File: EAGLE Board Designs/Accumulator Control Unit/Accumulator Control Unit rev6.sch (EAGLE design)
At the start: 261 parts, among them J1 CONNECTOR-12_MF_T_V_, J2 CONNECTOR-6_μF_T_V_BLACK, J3 CONNECTOR-4_μF_T_V_BLACK, J4 CONNECTOR-2_MF_T_V_, J5 CONNECTOR-8_μF_T_V_BLACK, J6 CONNECTOR-16_MF_T_V_, J9 CONNECTOR-2_MF_T_V_, Q1 TRANSISTOR_N_MOS__PMV15ENEA, Q2 TRANSISTOR_N_MOS__PMV15ENEA, Q3 TRANSISTOR_N_MOS__PMV15ENEA, Q4 TRANSISTOR_N_MOS__PMV15ENEA, T1 TRANSFORMER_HM2112ZNLT_AIRGAP, U1 VOLTAGE_REGULATOR_SOT-223_3.3V, U10 TCAN1051HQV-Q1, U11 OPAMP_1_CHANNEL_OPA991, U12 OPAMP_1_CHANNEL_OPA991, U13 OPAMP_1_CHANNEL_OPA991, U14 RELAY_SOLIDSTATE_NO_DIP-4, U15 LM555, U16 OPAMP_1_CHANNEL_OPA991, U17 MAX7404, U18 OPAMP_1_CHANNEL_OPA991, U19 MAX7404, U2 RELAY_SOLIDSTATE_NO_DIP-4, U20 LOGICGATE_BUFFER, U21 ADM8316WBX30, U22 OPAMP_1_CHANNEL_OPA991, U23 LOGICGATE_AND_DCK3, U24 LOGICGATE_AND_DCK3, U25 LOGICGATE_AND_DCK3, U26 OPAMP_1_CHANNEL_OPA991, U27 ADG1423, U28 OPAMP_1_CHANNEL_OPA991, U29 MAX7404, U3 RELAY_SOLIDSTATE_NO_DIP-4, U30 OPAMP_1_CHANNEL_OPA991, U31 MAX7404, U32 LTC6820, U33 OPAMP_1_CHANNEL_OPA991, U4 OPAMP_1_CHANNEL_OPA991, U5 OPAMP_1_CHANNEL_OPA991, U6 TCAN1051HQV-Q1, U7 LTC6820, U8 OPAMP_1_CHANNEL_OPA991, U9 OPAMP_1_CHANNEL_OPA991

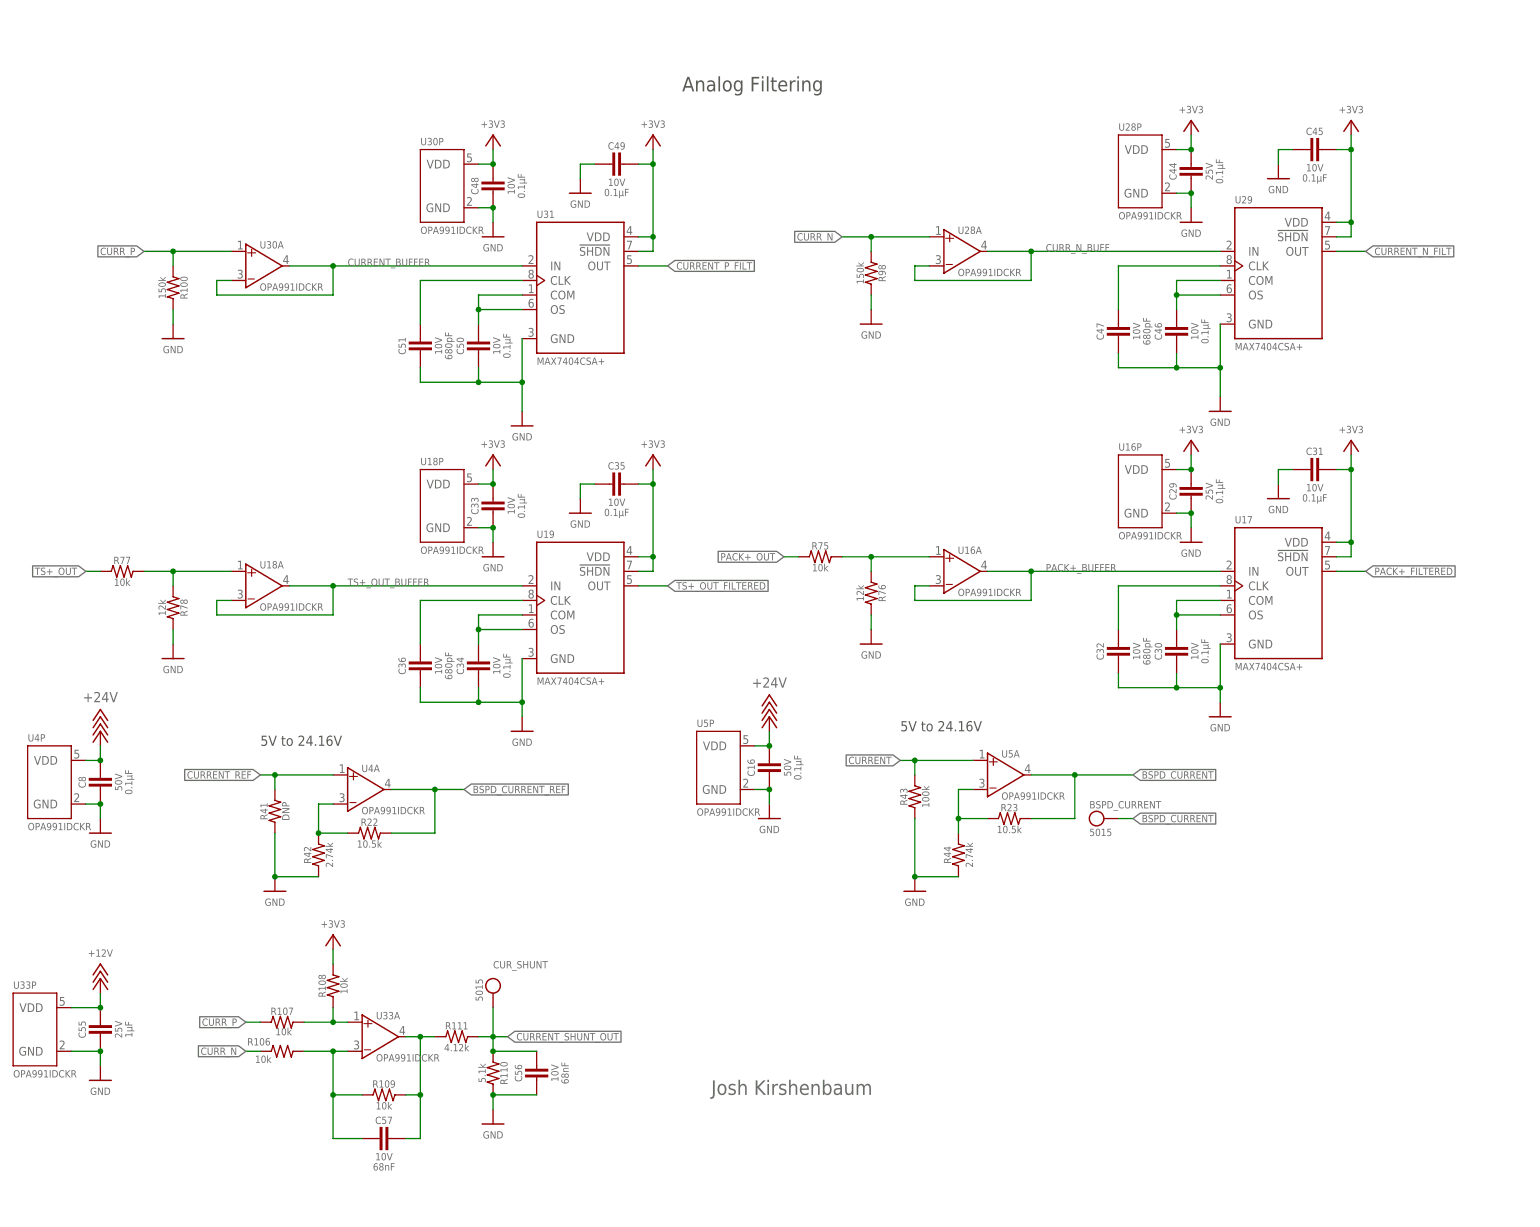
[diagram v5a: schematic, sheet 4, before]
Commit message: changed filters
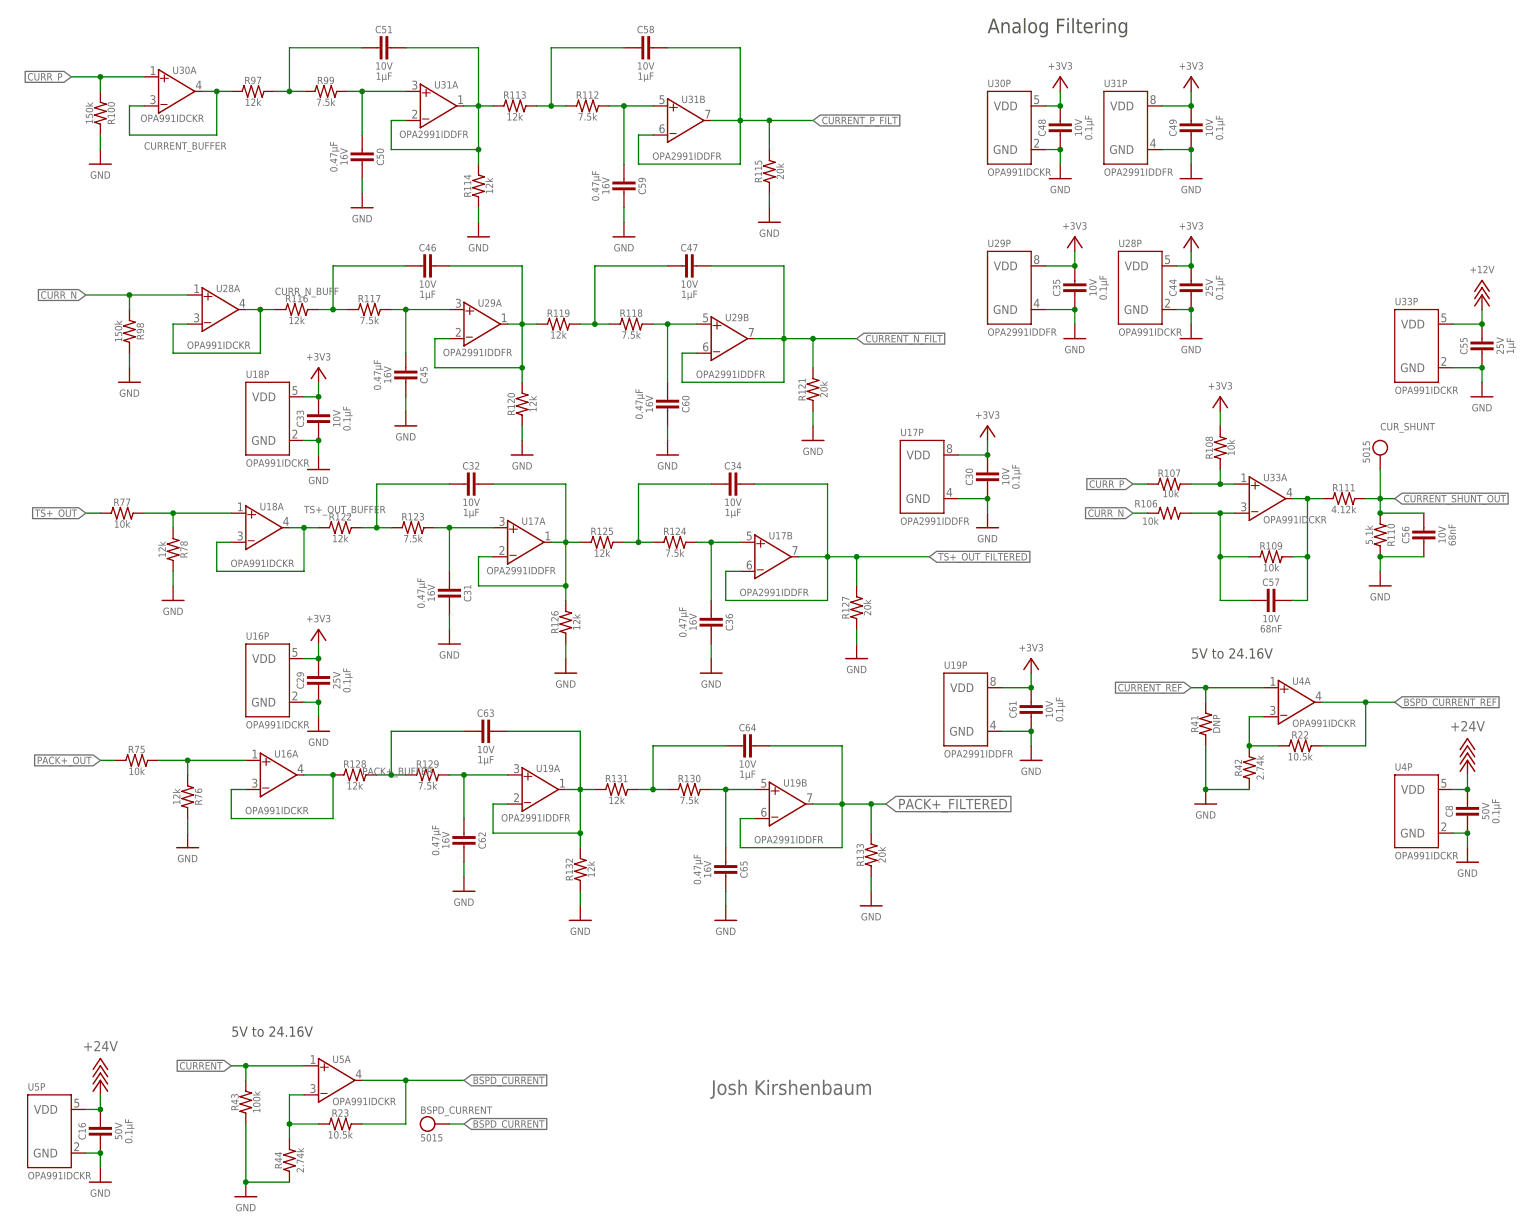
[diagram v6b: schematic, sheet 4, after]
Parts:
- added C58, C63, C64: CAPACITOR_0603_10V_1UF, HyTechDevices:CAPACITOR_0603_10V_1UF
- added C59, C60, C62, C65: CAPACITOR_0603_16V_0.47UF, HyTechDevices:CAPACITOR_0603_16V_0.47UF
- added C61: CAPACITOR_0603_10V_0.1UF, HyTechDevices - Copy:CAPACITOR_0603_10V_0.1UF
- added R112, R117, R118, R123, R124, R129, R130, R99: RESISTOR_0603_7.5K, HyTechDevices:RESISTOR_0603_7.5K
- added R113, R114, R116, R119, R120, R122, R125, R126, R128, R131, R132, R97: RESISTOR_0603_12K, HyTechDevices:RESISTOR_0603_12K
- added R115, R121, R127, R133: RESISTOR_0603_20K, HyTechDevices:RESISTOR_0603_20K
- C31, C45, C50: value CAPACITOR_0603_10V_0.1UF -> CAPACITOR_0603_16V_0.47UF; device HyTechDevices - Copy:CAPACITOR_0603_10V_0.1UF -> HyTechDevices:CAPACITOR_0603_16V_0.47UF
- C32, C47, C51: value CAPACITOR_0603_10V_680PF -> CAPACITOR_0603_10V_1UF; device HyTechDevices - Copy:CAPACITOR_0603_10V_680PF -> HyTechDevices:CAPACITOR_0603_10V_1UF
- C34, C46: value CAPACITOR_0603_10V_0.1UF -> CAPACITOR_0603_10V_1UF; device HyTechDevices - Copy:CAPACITOR_0603_10V_0.1UF -> HyTechDevices:CAPACITOR_0603_10V_1UF
- C36: value CAPACITOR_0603_10V_680PF -> CAPACITOR_0603_16V_0.47UF; device HyTechDevices - Copy:CAPACITOR_0603_10V_680PF -> HyTechDevices:CAPACITOR_0603_16V_0.47UF
- U17, U19, U29, U31: value MAX7404 -> OPAMP_2_CHANNEL_OPA_2991; device HyTechDevices:MAX7404 -> HyTechDevices:OPAMP_2_CHANNEL_OPA_2991
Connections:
- new net N$35: C47.2, R118.1, R119.2
- new net N$52: C58.2, R112.1, R113.2
- new net N$55: C59.1, R112.2, U31B.VIN+
- new net N$65: C51.2, R97.2, R99.1
- new net N$66: C51.1, R113.1, R114.2, U31A.VIN-, U31A.VOUT
- new net N$68: C45.1, R117.2, U29A.VIN+
- new net N$69: C50.1, R99.2, U31A.VIN+
- new net N$70: C64.2, R130.1, R131.2
- new net N$71: C65.1, R130.2, U19B.VIN+
- new net N$72: C63.2, R128.2, R129.1
- new net N$73: C63.1, R131.1, R132.2, U19A.VIN-, U19A.VOUT
- new net N$74: C62.1, R129.2, U19A.VIN+
- net +3V3: now also C30.1, C61.1, U17P.VDD, U19P.VDD, U29P.VDD, U31P.VDD; no longer C31.1, C45.1, U17.!SHDN, U17.VDD, U19.!SHDN, U19.VDD, U29.!SHDN, U29.VDD, U31.!SHDN, U31.VDD
- net CURRENT_BUFFER: now also R97.1; no longer U31.IN
- net CURRENT_N_FILT: now also C47.1, R121.2, U29B.VIN-, U29B.VOUT; no longer U29.OUT
- net CURRENT_P_FILT: now also C58.1, R115.2, U31B.VIN-, U31B.VOUT; no longer U31.OUT
- net CURR_N_BUFF: now also R116.1; no longer U29.IN
- net GND: now also C59.2, C60.2, C61.2, C62.2, C65.2, R114.1, R115.1, R120.1, R121.1, R126.1, R127.1, R132.1, R133.1, U17P.GND, U19P.GND, U29P.GND, U31P.GND; no longer C32.2, C34.2, C46.2, C47.2, C51.2, U17.GND, U19.GND, U29.GND, U31.GND
- net N$26: now also C34.2, R124.1, R125.2; no longer C34.1, U19.COM, U19.OS
- net N$45: now also R124.2, U17B.VIN+; no longer U19.CLK
- net N$50: now also C32.2, R122.2, R123.1; no longer C50.1, U31.COM, U31.OS
- net N$51: now also C60.1, R118.2, U29B.VIN+; no longer C51.1, U31.CLK
- net N$53: now also C46.2, R116.2, R117.1; no longer C46.1, U29.COM, U29.OS
- net N$54: now also C46.1, R119.1, R120.2, U29A.VIN-, U29A.VOUT; no longer C47.1, U29.CLK
- net N$56: now also C32.1, R125.1, R126.2, U17A.VIN-, U17A.VOUT; no longer C30.1, U17.COM, U17.OS
- net N$57: now also C31.1, R123.2, U17A.VIN+; no longer C32.1, U17.CLK
- net PACK+_BUFFER: now also R128.1; no longer U17.IN
- net PACK+_FILTERED: now also C64.1, R133.2, U19B.VIN-, U19B.VOUT; no longer U17.OUT
- net TS+_OUT_BUFFER: now also R122.1; no longer U19.IN
- net TS+_OUT_FILTERED: now also C34.1, R127.2, U17B.VIN-, U17B.VOUT; no longer U19.OUT
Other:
- moved on the sheet: BSPD_CURRENT, C16, C29, C30, C31, C32, C33, C34, C35, C36, C44, C45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

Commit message: swaped some of the pins around for easier routing
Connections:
- net ISO_PACK+: now also J5.2; no longer J5.1
- net ISO_PACK-: now also J5.1; no longer J5.2
- net ISO_TS+: now also J5.4; no longer J5.3
- net ISO_TS-: now also J5.3; no longer J5.4
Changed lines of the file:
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@@
 </segment>
 </net>
-<net name="ISO_PACK+" class="0">
+<net name="ISO_PACK-" class="0">
 <segment>
 <wire x1="20.32" y1="165.1" x2="22.86" y2="165.1" width="0.1524" layer="91"/>
@@
 </segment>
 </net>
-<net name="ISO_PACK-" class="0">
-<segment>
-<wire x1="20.32" y1="162.56" x2="22.86" y2="162.56" width="0.1524" layer="91"/>
-<label x="22.86" y="162.56" size="1.27" layer="95" xref="yes"/>
-<pinref part="J5" gate="G$1" pin="2"/>
-</segment>
-</net>
-<net name="ISO_TS+" class="0">
+<net name="ISO_TS-" class="0">
 <segment>
 <wire x1="20.32" y1="160.02" x2="22.86" y2="160.02" width="0.1524" layer="91"/>
 <label x="22.86" y="160.02" size="1.27" layer="95" xref="yes"/>
 <pinref part="J5" gate="G$1" pin="3"/>
-</segment>
-</net>
-<net name="ISO_TS-" class="0">
-<segment>
-<wire x1="20.32" y1="157.48" x2="22.86" y2="157.48" width="0.1524" layer="91"/>
-<label x="22.86" y="157.48" size="1.27" layer="95" xref="yes"/>
-<pinref part="J5" gate="G$1" pin="4"/>
 </segment>
 </net>
@@
 </segment>
 </net>
+<net name="ISO_TS+" class="0">
+<segment>
+<wire x1="20.32" y1="157.48" x2="22.86" y2="157.48" width="0.1524" layer="91"/>
+<label x="22.86" y="157.48" size="1.27" layer="95" xref="yes"/>
+<pinref part="J5" gate="G$1" pin="4"/>
+</segment>
+</net>
+<net name="ISO_PACK+" class="0">
+<segment>
+<wire x1="20.32" y1="162.56" x2="22.86" y2="162.56" width="0.1524" layer="91"/>
+<label x="22.86" y="162.56" size="1.27" layer="95" xref="yes"/>
+<pinref part="J5" gate="G$1" pin="2"/>
+</segment>
+</net>

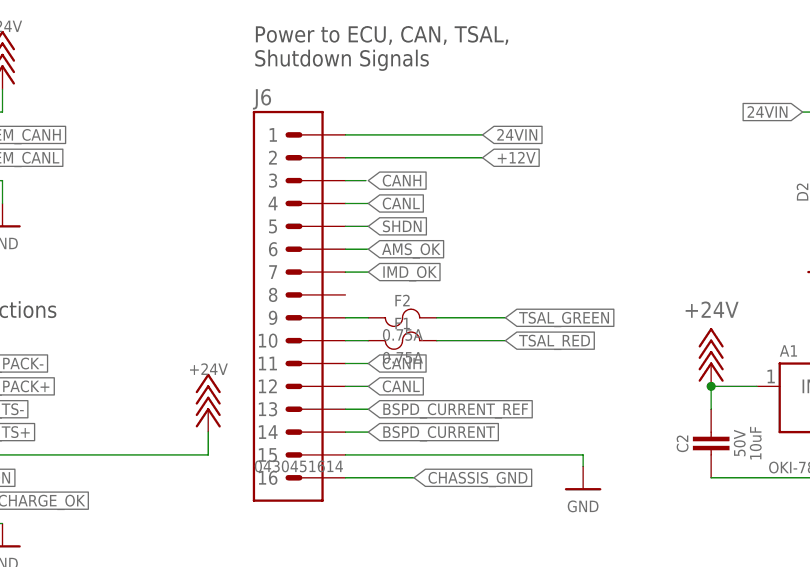
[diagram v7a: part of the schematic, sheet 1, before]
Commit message: moved can for better routing and almost done
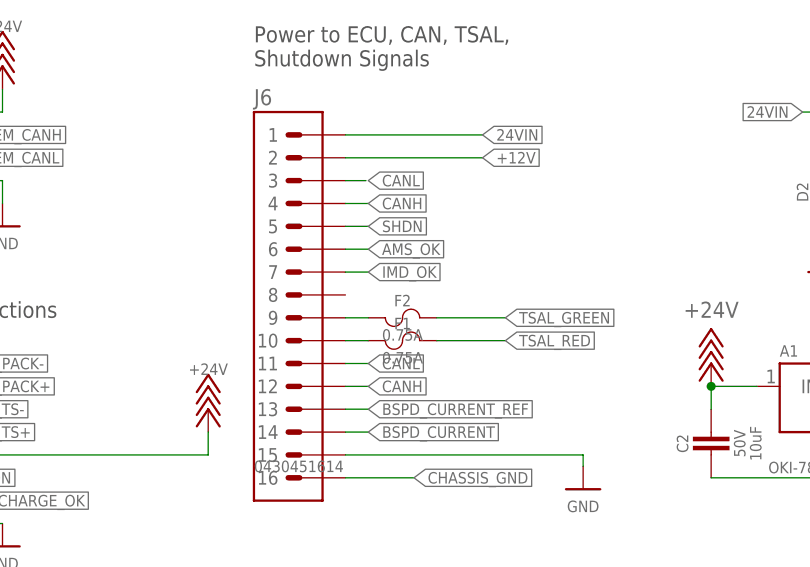
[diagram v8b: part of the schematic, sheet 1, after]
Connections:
- net CANH: now also J6.12, J6.4; no longer J6.11, J6.3
- net CANL: now also J6.11, J6.3; no longer J6.12, J6.4
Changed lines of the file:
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@@
 <net name="CANH" class="0">
+<segment>
+<pinref part="J6" gate="G$1" pin="12"/>
+<wire x1="66.04" y1="162.56" x2="68.58" y2="162.56" width="0.1524" layer="91"/>
+<label x="68.58" y="162.56" size="1.27" layer="95" xref="yes"/>
+</segment>
+<segment>
+<pinref part="J6" gate="G$1" pin="4"/>
+<wire x1="66.04" y1="182.88" x2="68.58" y2="182.88" width="0.1524" layer="91"/>
+<label x="68.58" y="182.88" size="1.27" layer="95" xref="yes"/>
+</segment>
+</net>
+<net name="CANL" class="0">
 <segment>
 <pinref part="J6" gate="G$1" pin="11"/>
@@
 </segment>
 </net>
-<net name="CANL" class="0">
-<segment>
-<pinref part="J6" gate="G$1" pin="4"/>
-<wire x1="66.04" y1="182.88" x2="68.58" y2="182.88" width="0.1524" layer="91"/>
-<label x="68.58" y="182.88" size="1.27" layer="95" xref="yes"/>
-</segment>
-<segment>
-<pinref part="J6" gate="G$1" pin="12"/>
-<wire x1="66.04" y1="162.56" x2="68.58" y2="162.56" width="0.1524" layer="91"/>
-<label x="68.58" y="162.56" size="1.27" layer="95" xref="yes"/>
-</segment>
-</net>
